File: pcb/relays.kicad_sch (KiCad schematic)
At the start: 80 parts, among them CN11 KF2EDGR-3.5-3P, CN12 KF2EDGR-3.5-3P, CN13 KF2EDGR-3.5-3P, CN15 KF2EDGR-3.5-3P, CN16 KF2EDGR-3.5-3P, CN17 KF2EDGR-3.5-3P, CN7 KF2EDGR-3.5-3P, CN9 KF2EDGR-3.5-3P, K1 Relay_SPDT, K2 Relay_SPDT, K3 Relay_SPDT, K4 Relay_SPDT, K5 Relay_SPDT, K6 Relay_SPDT, K7 Relay_SPDT, K8 Relay_SPDT, Q1 S8050, Q2 S8050, Q3 S8050, Q4 S8050, Q5 S8050, Q6 S8050, Q7 S8050, Q8 S8050, U1 PC817, U2 PC817, U3 PC817, U4 PC817, U5 PC817, U6 PC817, U7 PC817, U8 PC817

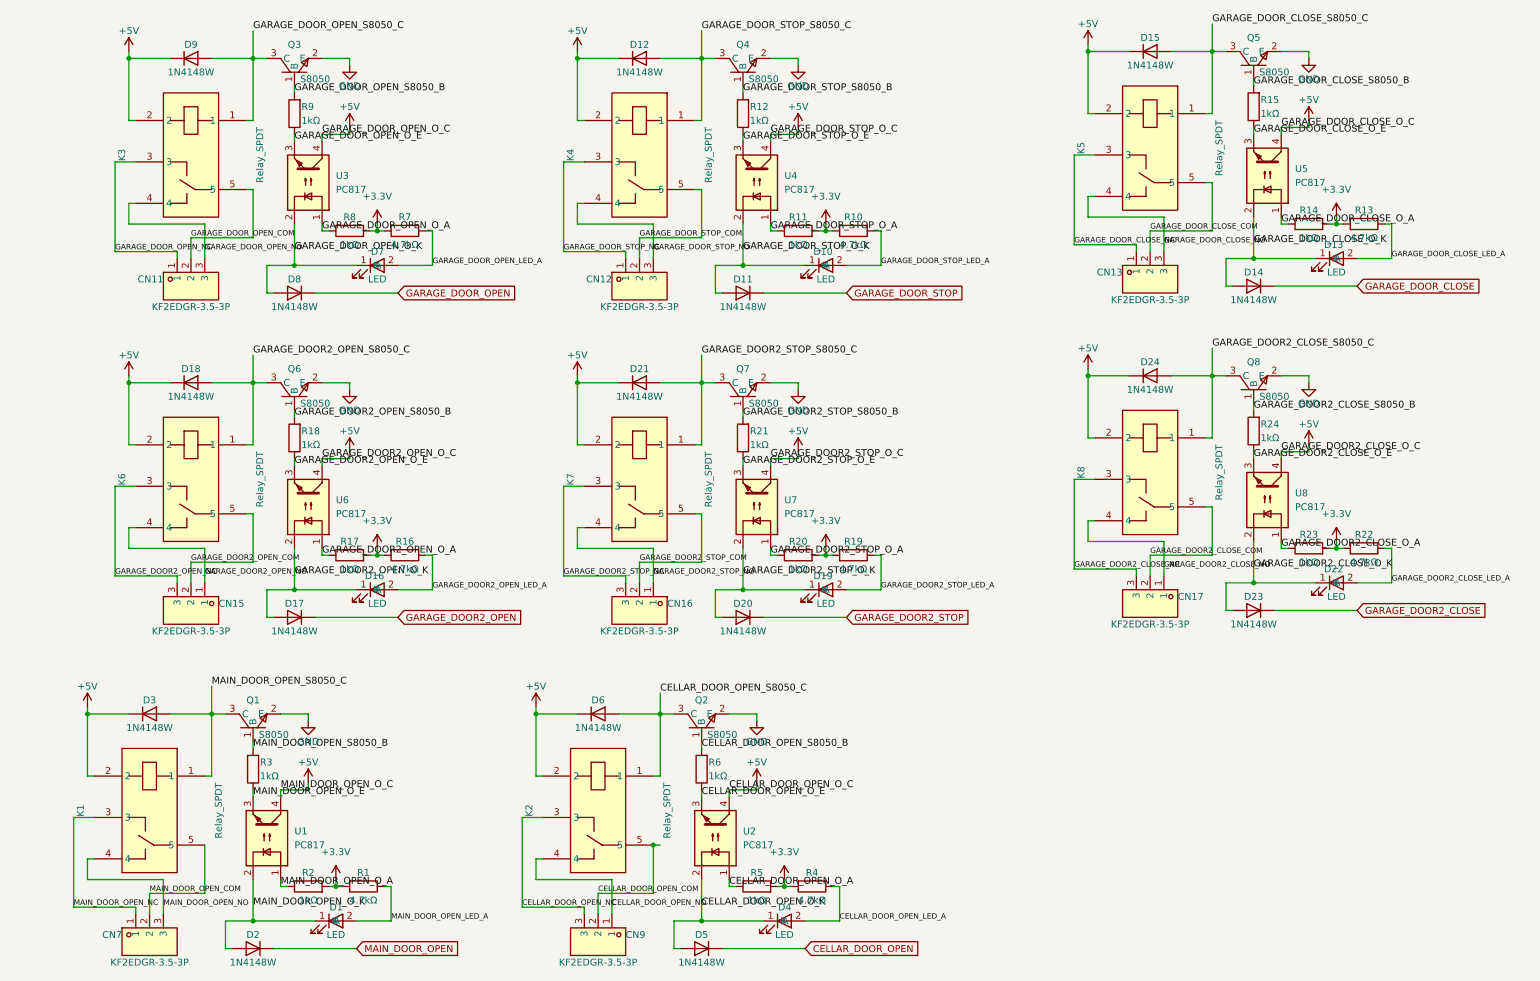
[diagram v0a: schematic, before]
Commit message: Improve PCB layout and connectors.
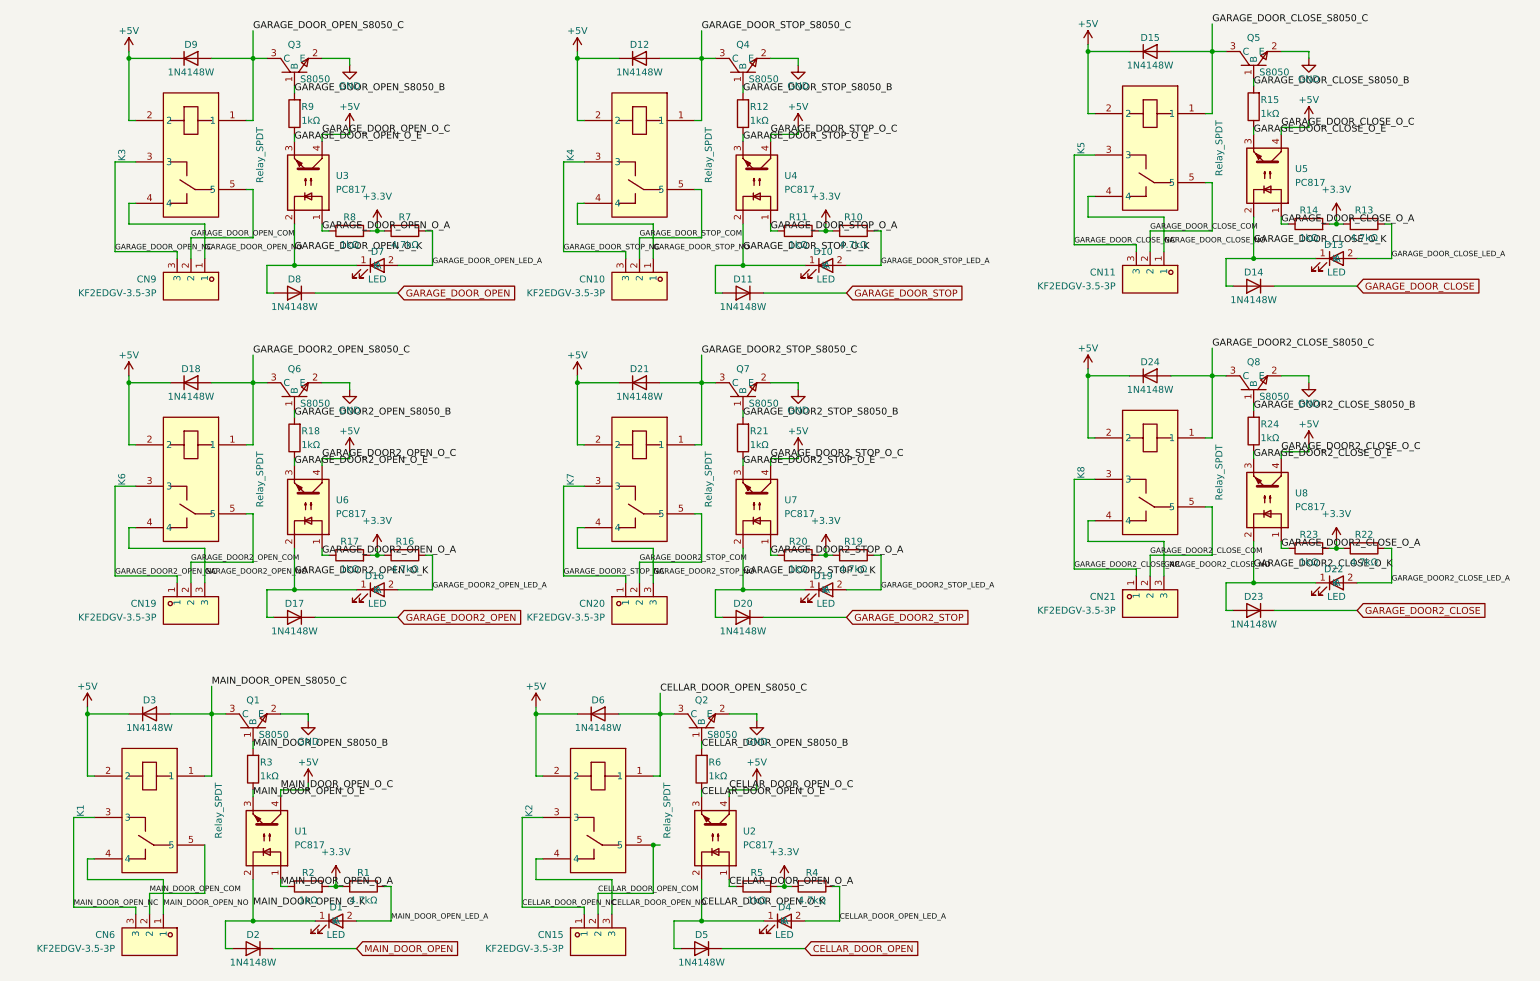
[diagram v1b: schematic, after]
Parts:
- CN10: renamed from CN12; value KF2EDGR-3.5-3P -> KF2EDGV-3.5-3P; footprint easyeda2kicad:CONN-TH_3P-P3.50_KF2EDGR-3.5-3P -> easyeda2kicad:CONN-TH_3P-P3.50_KF2EDGV-3.5-3P; symbol easyeda2kicad:KF2EDGR-3.5-3P -> easyeda2kicad:KF2EDGV-3.5-3P; LCSC Part C441172 -> C441322
- CN11: renamed from CN13; value KF2EDGR-3.5-3P -> KF2EDGV-3.5-3P; footprint easyeda2kicad:CONN-TH_3P-P3.50_KF2EDGR-3.5-3P -> easyeda2kicad:CONN-TH_3P-P3.50_KF2EDGV-3.5-3P; symbol easyeda2kicad:KF2EDGR-3.5-3P -> easyeda2kicad:KF2EDGV-3.5-3P; LCSC Part C441172 -> C441322
- CN15: renamed from CN9; value KF2EDGR-3.5-3P -> KF2EDGV-3.5-3P; footprint easyeda2kicad:CONN-TH_3P-P3.50_KF2EDGR-3.5-3P -> easyeda2kicad:CONN-TH_3P-P3.50_KF2EDGV-3.5-3P; symbol easyeda2kicad:KF2EDGR-3.5-3P -> easyeda2kicad:KF2EDGV-3.5-3P; LCSC Part C441172 -> C441322
- CN19: renamed from CN15; value KF2EDGR-3.5-3P -> KF2EDGV-3.5-3P; footprint easyeda2kicad:CONN-TH_3P-P3.50_KF2EDGR-3.5-3P -> easyeda2kicad:CONN-TH_3P-P3.50_KF2EDGV-3.5-3P; symbol easyeda2kicad:KF2EDGR-3.5-3P -> easyeda2kicad:KF2EDGV-3.5-3P; LCSC Part C441172 -> C441322
- CN20: renamed from CN16; value KF2EDGR-3.5-3P -> KF2EDGV-3.5-3P; footprint easyeda2kicad:CONN-TH_3P-P3.50_KF2EDGR-3.5-3P -> easyeda2kicad:CONN-TH_3P-P3.50_KF2EDGV-3.5-3P; symbol easyeda2kicad:KF2EDGR-3.5-3P -> easyeda2kicad:KF2EDGV-3.5-3P; LCSC Part C441172 -> C441322
- CN21: renamed from CN17; value KF2EDGR-3.5-3P -> KF2EDGV-3.5-3P; footprint easyeda2kicad:CONN-TH_3P-P3.50_KF2EDGR-3.5-3P -> easyeda2kicad:CONN-TH_3P-P3.50_KF2EDGV-3.5-3P; symbol easyeda2kicad:KF2EDGR-3.5-3P -> easyeda2kicad:KF2EDGV-3.5-3P; LCSC Part C441172 -> C441322
- CN6: renamed from CN7; value KF2EDGR-3.5-3P -> KF2EDGV-3.5-3P; footprint easyeda2kicad:CONN-TH_3P-P3.50_KF2EDGR-3.5-3P -> easyeda2kicad:CONN-TH_3P-P3.50_KF2EDGV-3.5-3P; symbol easyeda2kicad:KF2EDGR-3.5-3P -> easyeda2kicad:KF2EDGV-3.5-3P; LCSC Part C441172 -> C441322
- CN9: renamed from CN11; value KF2EDGR-3.5-3P -> KF2EDGV-3.5-3P; footprint easyeda2kicad:CONN-TH_3P-P3.50_KF2EDGR-3.5-3P -> easyeda2kicad:CONN-TH_3P-P3.50_KF2EDGV-3.5-3P; symbol easyeda2kicad:KF2EDGR-3.5-3P -> easyeda2kicad:KF2EDGV-3.5-3P; LCSC Part C441172 -> C441322
- R1, R10, R13, R16, R19, R22, R4, R7: LCSC Part C3017854 -> C103059
- R11, R12, R14, R15, R17, R18, R2, R20, R21, R23, R24, R3, R5, R6, R8: LCSC C3017842 -> (none); LCSC Part (none) -> C3017842
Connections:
- net CELLAR_DOOR_OPEN_NC: now also CN15.1; no longer CN15.3
- net CELLAR_DOOR_OPEN_NO: now also CN15.3; no longer CN15.1
- net GARAGE_DOOR2_CLOSE_NC: now also CN21.1; no longer CN21.3
- net GARAGE_DOOR2_CLOSE_NO: now also CN21.3; no longer CN21.1
- net GARAGE_DOOR2_OPEN_NC: now also CN19.1; no longer CN19.3
- net GARAGE_DOOR2_OPEN_NO: now also CN19.3; no longer CN19.1
- net GARAGE_DOOR2_STOP_NC: now also CN20.1; no longer CN20.3
- net GARAGE_DOOR2_STOP_NO: now also CN20.3; no longer CN20.1
- net GARAGE_DOOR_CLOSE_NC: now also CN11.3; no longer CN11.1
- net GARAGE_DOOR_CLOSE_NO: now also CN11.1; no longer CN11.3
- net GARAGE_DOOR_OPEN_NC: now also CN9.3; no longer CN9.1
- net GARAGE_DOOR_OPEN_NO: now also CN9.1; no longer CN9.3
- net GARAGE_DOOR_STOP_NC: now also CN10.3; no longer CN10.1
- net GARAGE_DOOR_STOP_NO: now also CN10.1; no longer CN10.3
- net MAIN_DOOR_OPEN_NC: now also CN6.3; no longer CN6.1
- net MAIN_DOOR_OPEN_NO: now also CN6.1; no longer CN6.3
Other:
- moved on the sheet: CN10, CN11, CN15, CN19, CN20, CN21, CN6, CN9
